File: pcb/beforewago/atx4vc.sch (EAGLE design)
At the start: 69 parts, among them IC2 REG1117, IC3 STM32F042F4, IC4 MY_7905DT, J1 ATX24RH, SW1 324_SW, SW2 324_SW, SW3 324_SW, SW4 324_SW, SW5 324_SW, SW7 324_SW, U1 USBC_16P, U2 USBC_16P

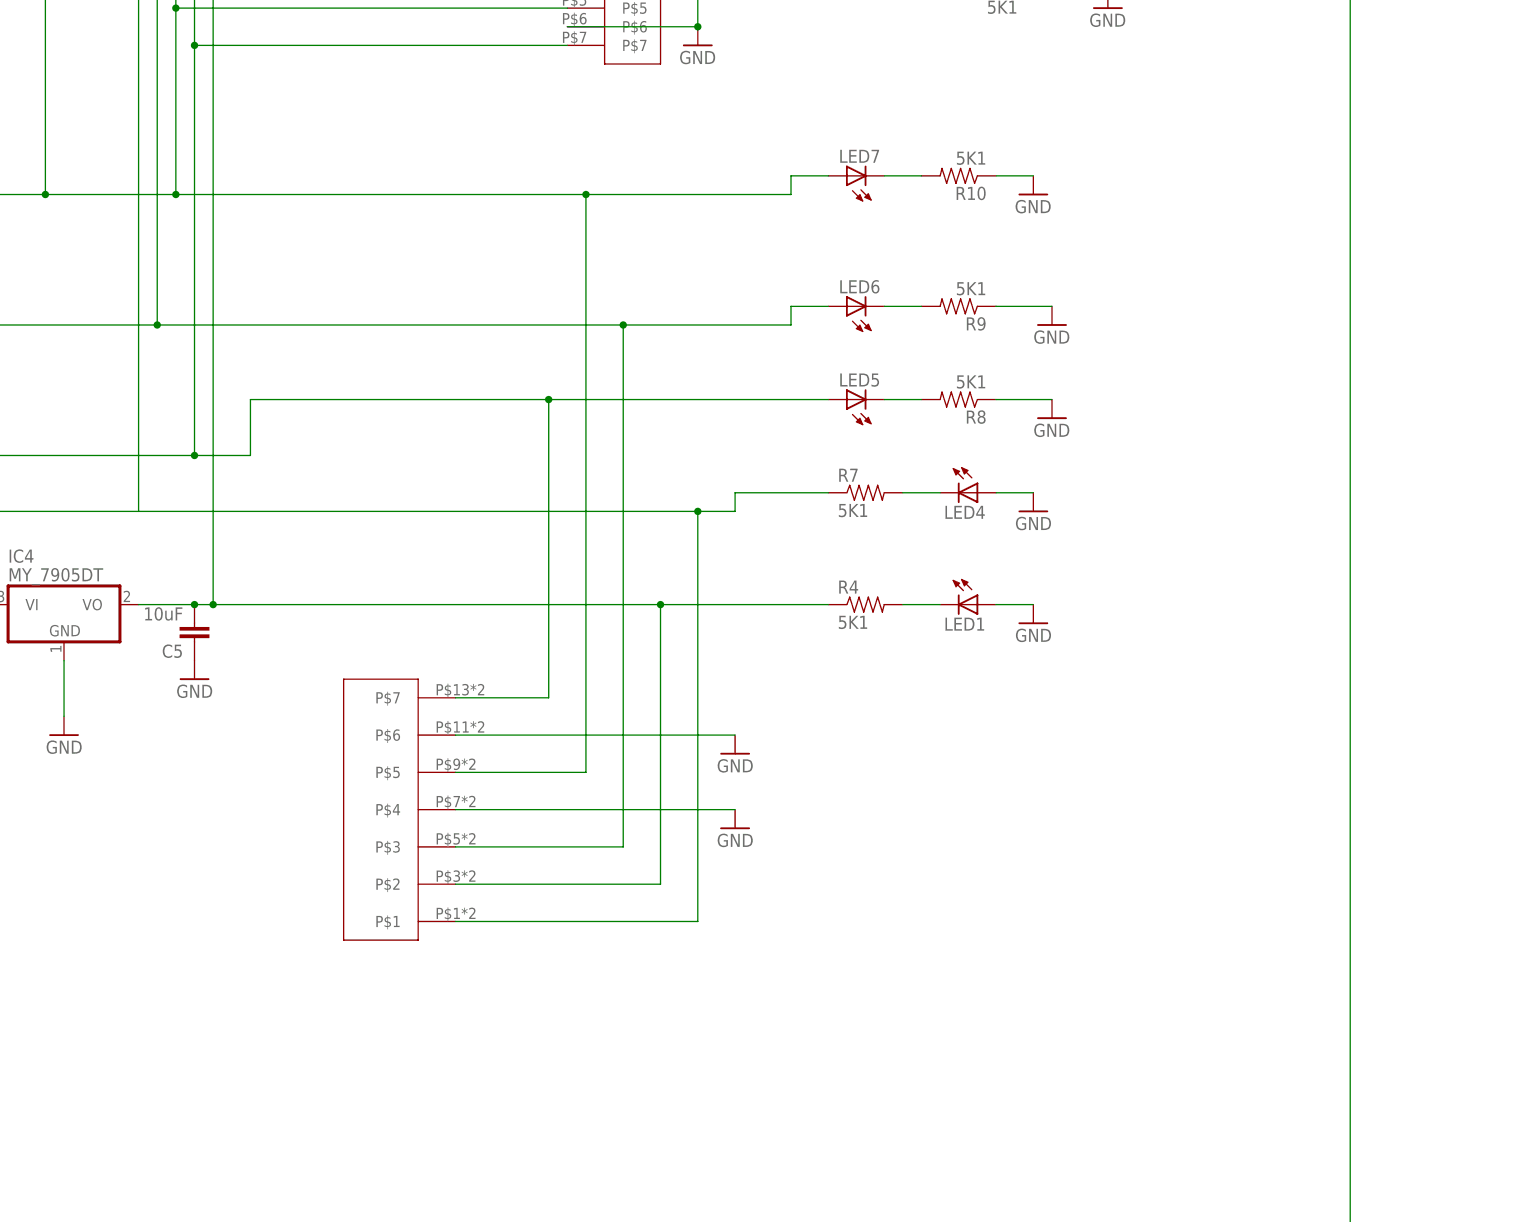
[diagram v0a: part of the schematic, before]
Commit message: switched to WAGO connectors
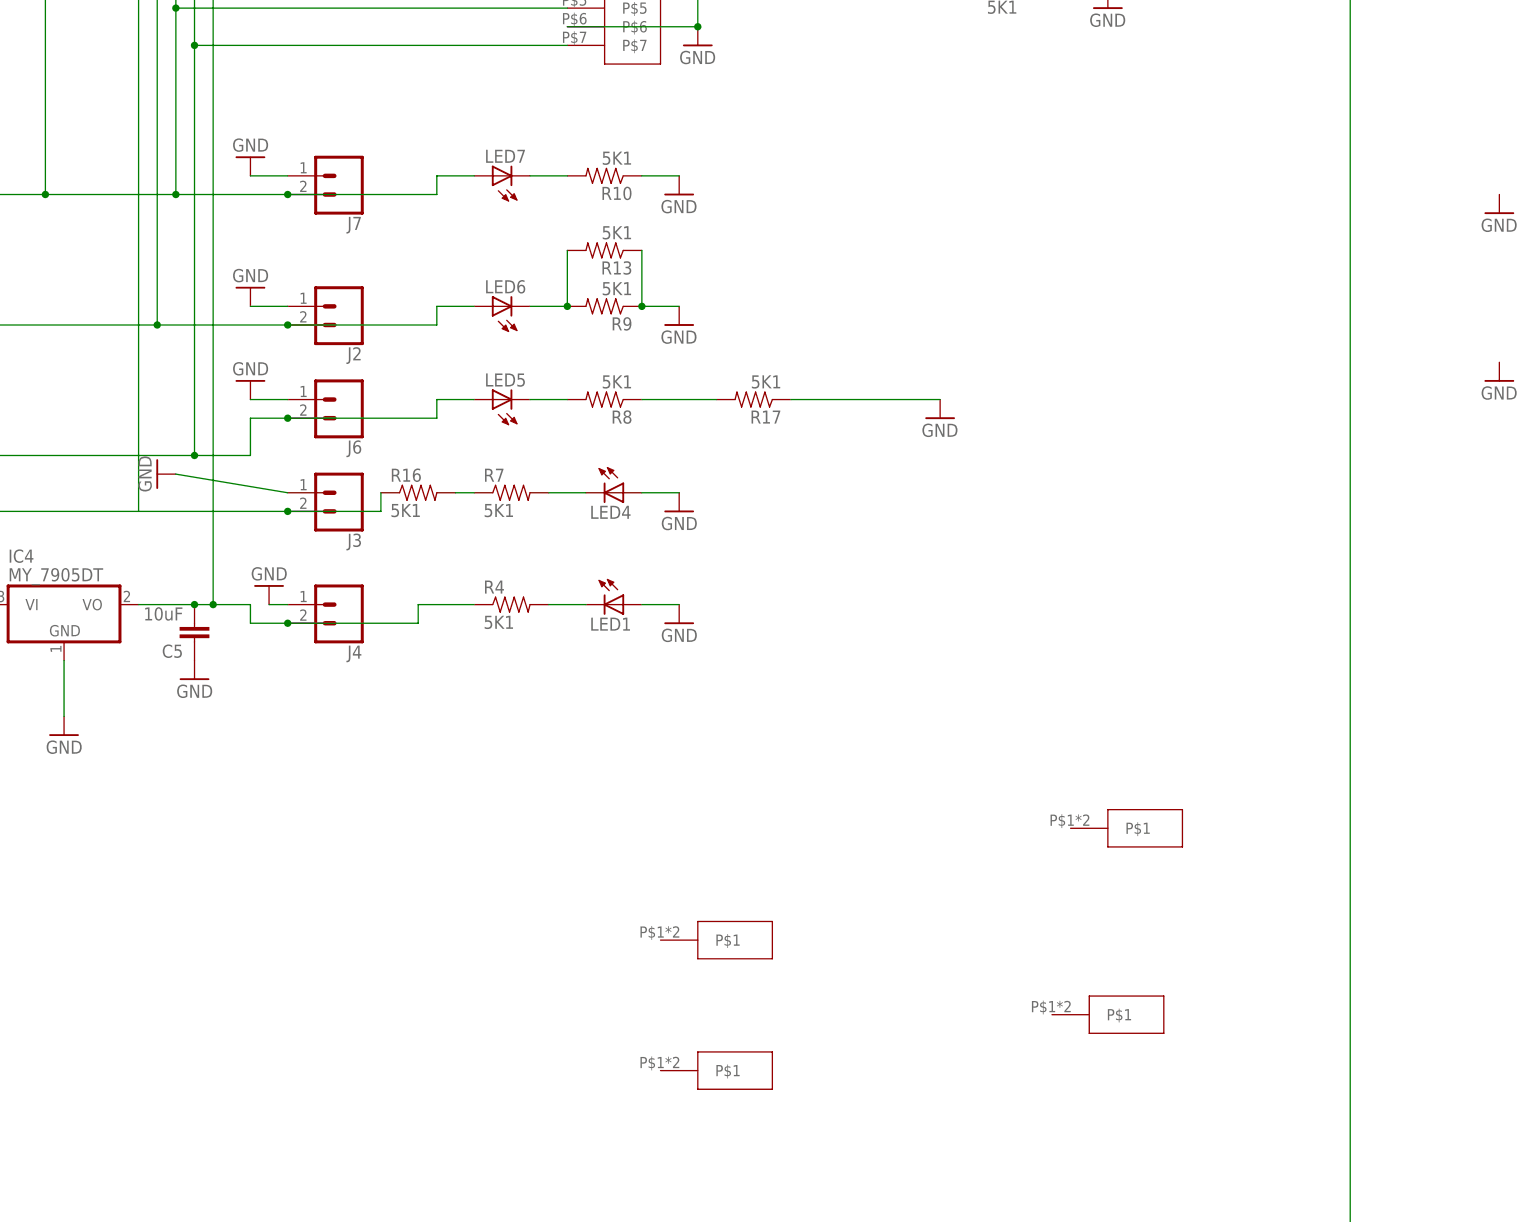
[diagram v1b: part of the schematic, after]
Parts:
- added J2, J3, J4, J6: (no value), atx_power_control:CONN_023.5MM
- added J7: (no value), atx_power_control:CONN_023.5MM-NO_SILK
- added R13, R17: 5K1, atx_power_control:RESISTOR0805-RES
- added R16: 5K1, SparkFun-Passives:RESISTOR0805-RES
- added U$11, U$12, U$13: WAGO257, atx4vc:WAGO257
- U$9: value WAGO257-7 -> WAGO257; device atx4vc:WAGO257-7 -> atx4vc:WAGO257
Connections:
- removed net -12V: IC4.VI, J1.-12V, R7.1, U$4.P$1, U$9.P$1
- removed net -5V: C5.2, IC4.VO, R4.1, U$4.P$2, U$9.P$2
- new net N$11: C5.2, IC4.VO, J4.2, R4.1, U$4.P$2
- new net N$2: IC4.VI, J1.-12V, J3.2, R16.1, U$4.P$1
- new net N$28: R16.2, R7.1
- new net N$32: R17.2, R8.1
- net F12V: now also J6.2; no longer U$9.P$7
- net F3V3: now also J2.2; no longer U$9.P$3
- net F5V: now also J7.2; no longer U$9.P$5
- net GND: now also J2.1, J3.1, J4.1, J6.1, J7.1, R13.1, R17.1; no longer R8.1, U$9.P$4, U$9.P$6
- net N$18: now also R13.2
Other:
- moved on the sheet: LED1, LED4, LED5, LED6, LED7, R10, R4, R7, R8, R9
